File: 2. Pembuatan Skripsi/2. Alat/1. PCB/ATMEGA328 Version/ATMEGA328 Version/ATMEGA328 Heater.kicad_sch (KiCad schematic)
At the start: 64 parts, among them J1 Conn_01x02, J2 Sensors, J3 Screw_Terminal_01x02, J5 FTDI, J6 Conn_02x04_Top_Bottom, K1 EE2-4.5NU, Q1 S9013, Q2 S9013, Q3 S9013, Q4 MMBT2222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

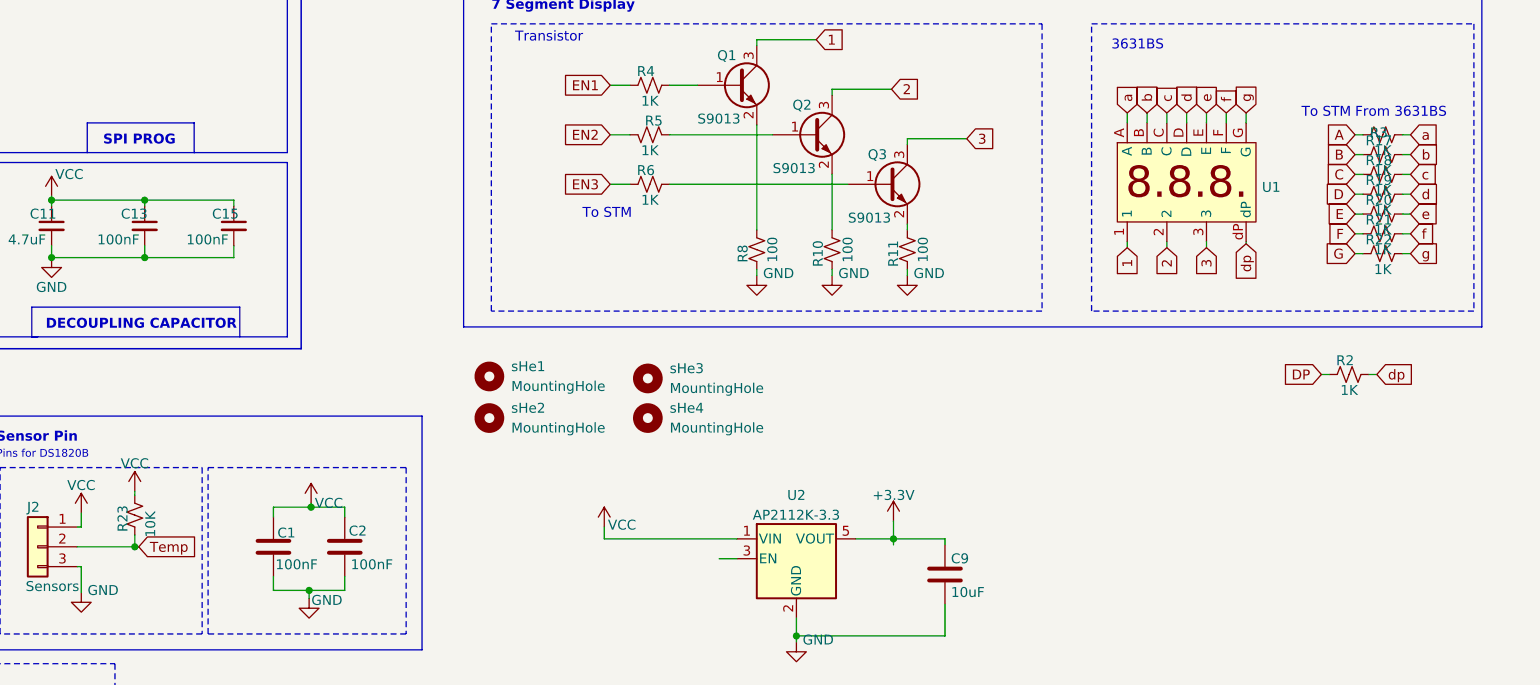
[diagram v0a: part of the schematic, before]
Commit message: Huge update for ATMEGA328P Board
Program is fully working:

- Get parameter, sensor data, led status, relay status.
- Show parameter on SevSeg
- Connected to NodeRed
- Board design is revised based on actual board
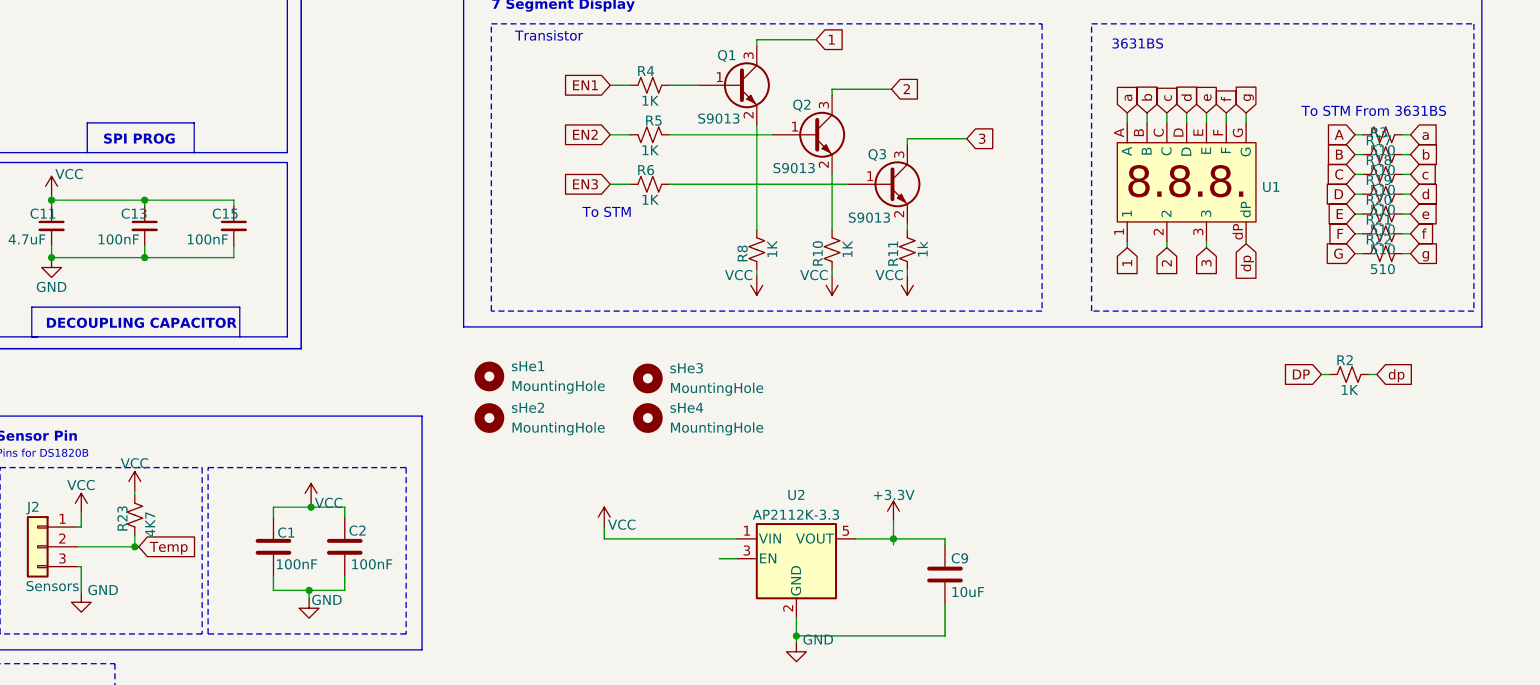
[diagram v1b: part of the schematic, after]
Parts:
- R10, R8: value 100 -> 1K
- R11: value 100 -> 1k
- R17, R18, R19, R20, R21, R22, R3: value 1K -> 510
- R23: value 10K -> 4K7
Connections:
- net GND: no longer R10.2, R11.2, R8.2
- net VCC: now also R10.2, R11.2, R8.2
